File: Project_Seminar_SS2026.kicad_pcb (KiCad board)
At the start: 6 copper layers, 117.3 x 75 mm, 122 parts, among them U1 MAX49925, U10 ADS8329IPW, U11 ADS8329IPW, U12 WPME-CDIP_18024115401, U13 WPME-CDIP_18024115401, U15 AD8032, U2 AD8032, U4 ASC37010LLZATR, U5 AD80301, U6 ADA4099-1, U7 MAX6070AAUT21, U8 MAX6070AAUT21, U9 MAX6070AAUT21, X1 WE74650073, X10 AKL_073-2, X2 WE74650073, X3 WE74650073, X4 MPE-087, X5 RTM1_3, X6 RTM1_3, X7 AKL_073-2, X8 BCS-122-L-S-TE_L, X9 BCS-122-L-S-TE

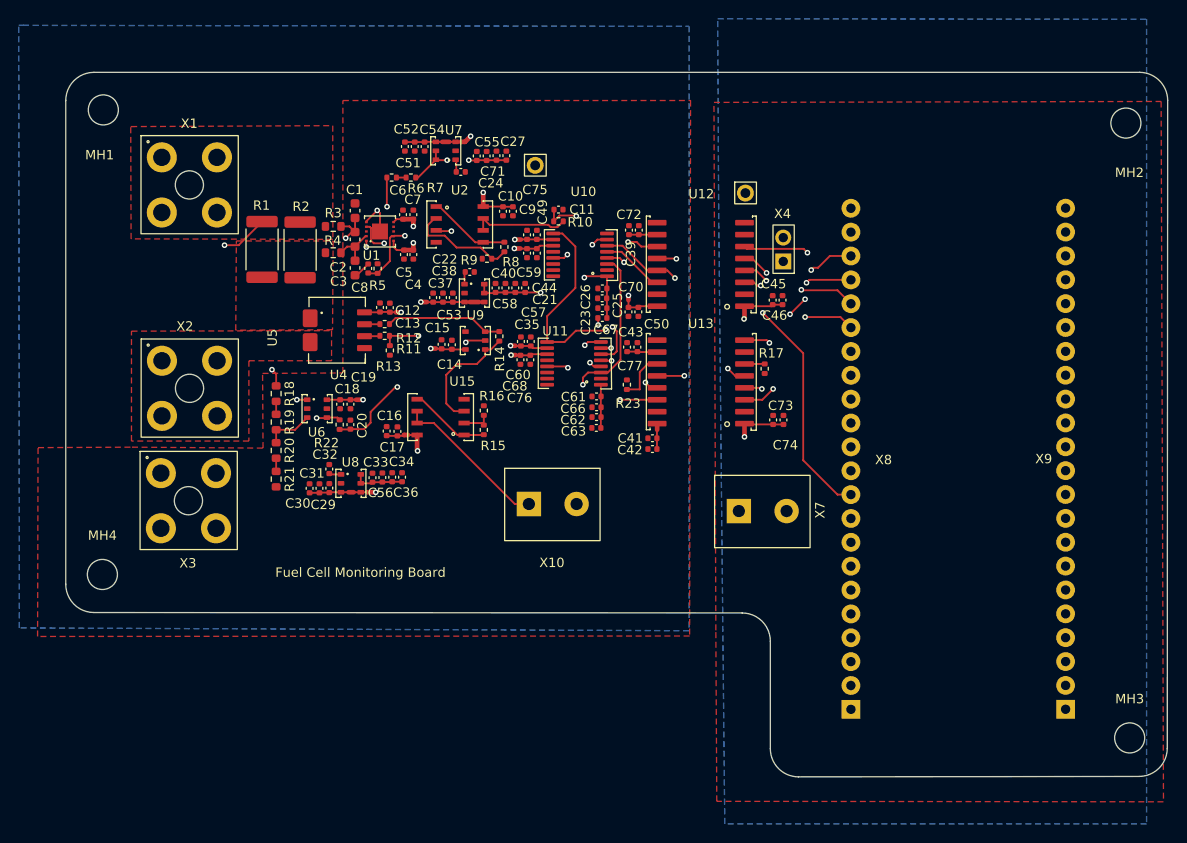
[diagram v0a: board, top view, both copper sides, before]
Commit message: Updated PCB design of Solder mask
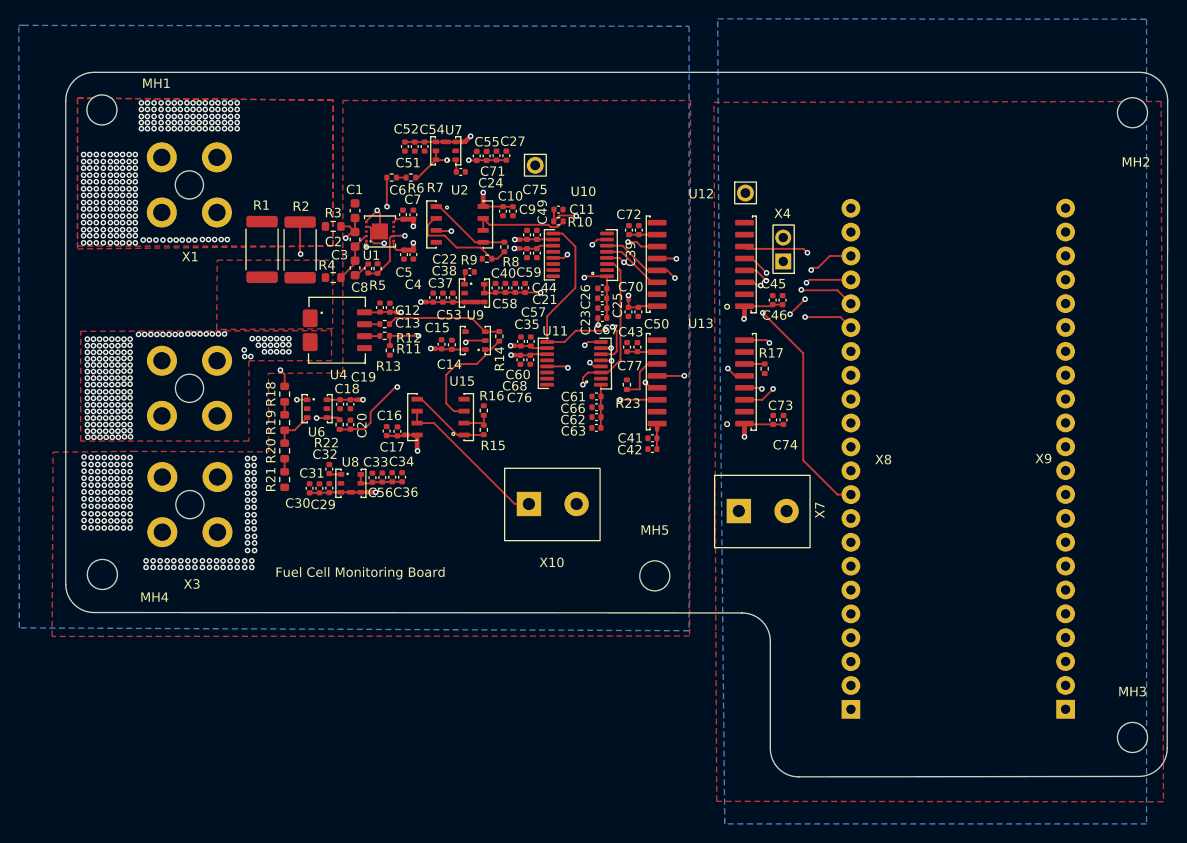
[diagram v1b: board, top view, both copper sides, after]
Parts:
- added MH5: MountingHole_3.2mm_M3, MountingHole:MountingHole_3.2mm_M3, F.Cu at (147.7, 98.6)
- moved R4 2.65 mm to (113.5, 66.8)
- moved MH2 1.30 mm to (198.6, 49.3)
- moved R19 0.91 mm to (108.3, 82.3)
- moved R18 0.91 mm to (108.3, 79.2)
- moved R20 0.91 mm to (108.3, 85.3)
- moved R21 0.91 mm to (108.3, 88.3)
- moved X3 0.44 mm to (98.2, 91.0)
- moved MH3 0.30 mm to (198.6, 115.8)
- moved MH1 0.15 mm to (88.8, 49.0)
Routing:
- net FC+: track 22.4 -> 18.6 mm, vias 2 -> 222
- net Net-(U6-+IN): track 5.22 -> 4.33 mm
- net /Fuel cell current measurement (page 2)/Vsn: track 4.93 -> 5.59 mm
- net GNDA: vias 3 -> 151
- net /Fuel cell current measurement (page 2)/LOAD: vias 0 -> 164
- added copper zone on In4.Cu, net /Fuel cell current measurement (page 2)/LOAD
- added copper zone on In4.Cu, net FC+
